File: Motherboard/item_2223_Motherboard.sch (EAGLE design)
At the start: 50 parts, among them IC1 MCP602SN, IC2 LD117AS33TR, IC4 MCP6S26, U1 ESP32-DEVKITC-32D, U2 ADS1256_BOARD, U3 SSD1306_128X64, X1 MSTBA4, X2 MSTBA4

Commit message: Correggi errore tipografico in item_2223_Motherboard.sch
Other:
- note added: "Lista Test Points: TP1 - ingresso Accel_0 TP2 - Accel_0 con bias TP3 - uscita PGA Accel_0/1 TP4 - uscita LPF Accel_0/AIN0+ TP5 - ingresso Accel_1 TP6 - Accel_1 con bias TP9 - ADC_HALF_VREF TP10 - +3V3 TP11 - +5V TP12 - GND"
- note removed: "Lista Tesp Points: TP1 - ingresso Accel_0 TP2 - Accel_0 con bias TP3 - uscita PGA Accel_0/1 TP4 - uscita LPF Accel_0/AIN0+ TP5 - ingresso Accel_1 TP6 - Accel_1 con bias TP9 - ADC_HALF_VREF TP10 - +3V3 TP11 - +5V TP12 - GND"
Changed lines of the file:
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@@
 Condizionamento coppie</text>
 <text x="346.71" y="20.32" size="2.54" layer="97">ISIS Bassa Friulana</text>
-<text x="289.56" y="33.02" size="2.1844" layer="97">Lista Tesp Points:
+<text x="289.56" y="33.02" size="2.1844" layer="97">Lista Test Points:
 TP1 - ingresso Accel_0
 TP2 - Accel_0 con bias

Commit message: Corretto GND di SSD1306 in Frontend e Motherboard
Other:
- moved on the sheet: U3
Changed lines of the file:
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@@
 <?xml version="1.0" encoding="utf-8"?>
 <!DOCTYPE eagle SYSTEM "eagle.dtd">
-<eagle version="9.6.2">
+<eagle version="7.7.0">
 <drawing>
 <settings>
 <setting alwaysvectorfont="no"/>
-<setting keepoldvectorfont="yes"/>
 <setting verticaltext="up"/>
 </settings>
-<grid distance="0.1" unitdist="inch" unit="inch" style="lines" multiple="1" display="yes" altdistance="0.01" altunitdist="inch" altunit="inch"/>
+<grid distance="0.1" unitdist="inch" unit="inch" style="lines" multiple="1" display="no" altdistance="0.01" altunitdist="inch" altunit="inch"/>
 <layers>
 <layer number="1" name="Top" color="4" fill="1" visible="no" active="no"/>

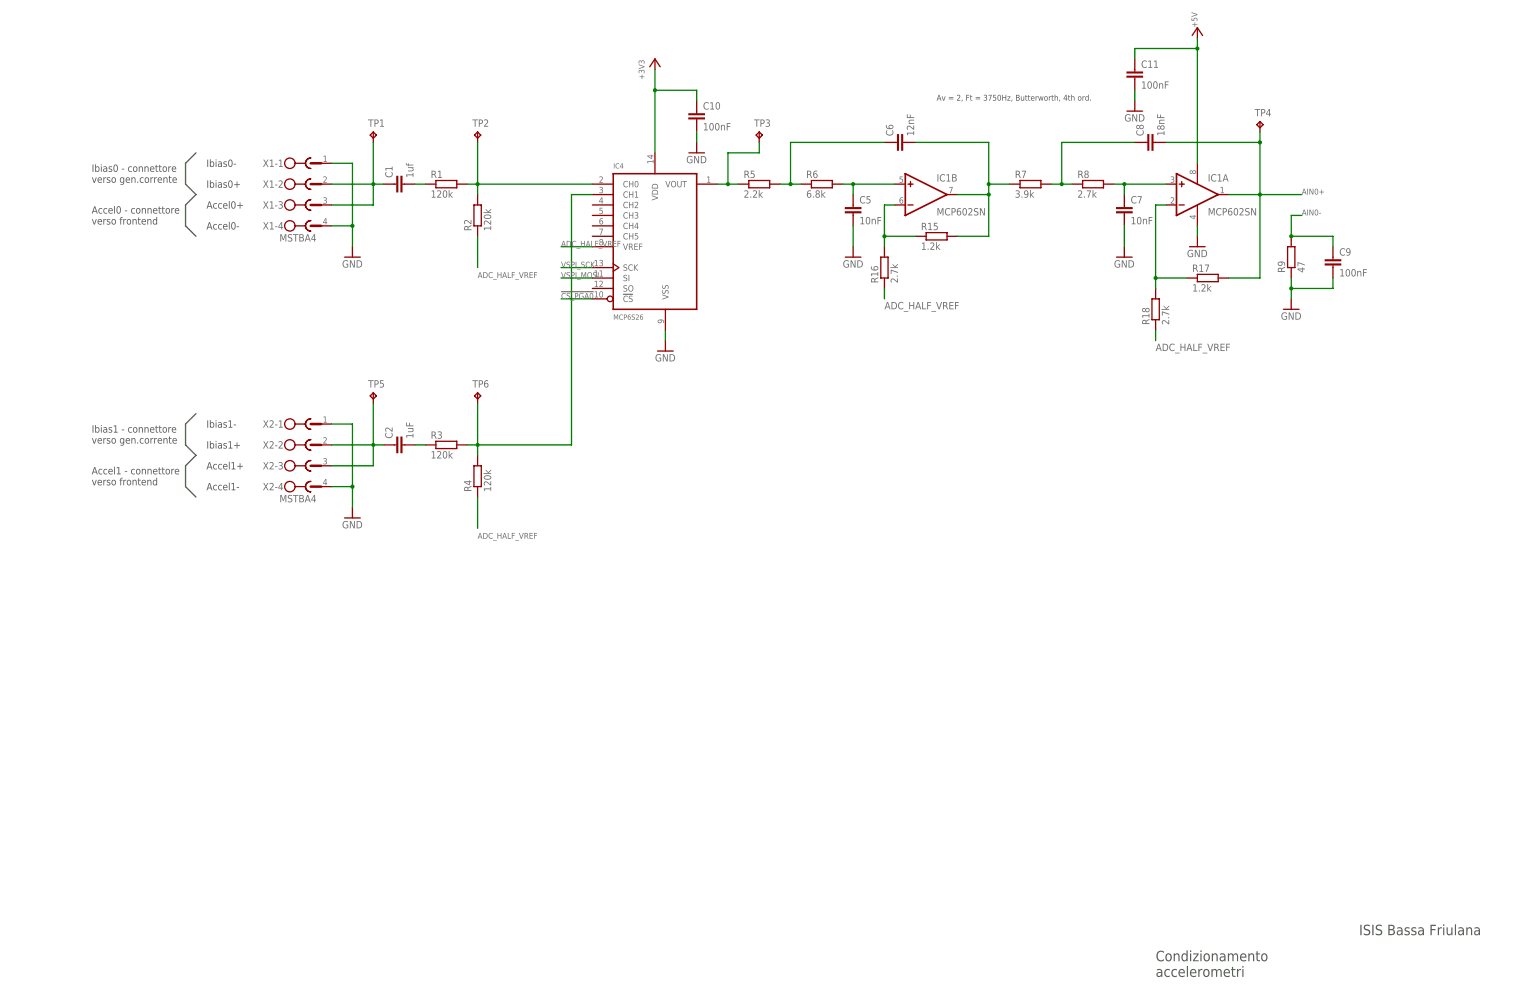
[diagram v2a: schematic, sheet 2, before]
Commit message: ingresso differenziale e AGND
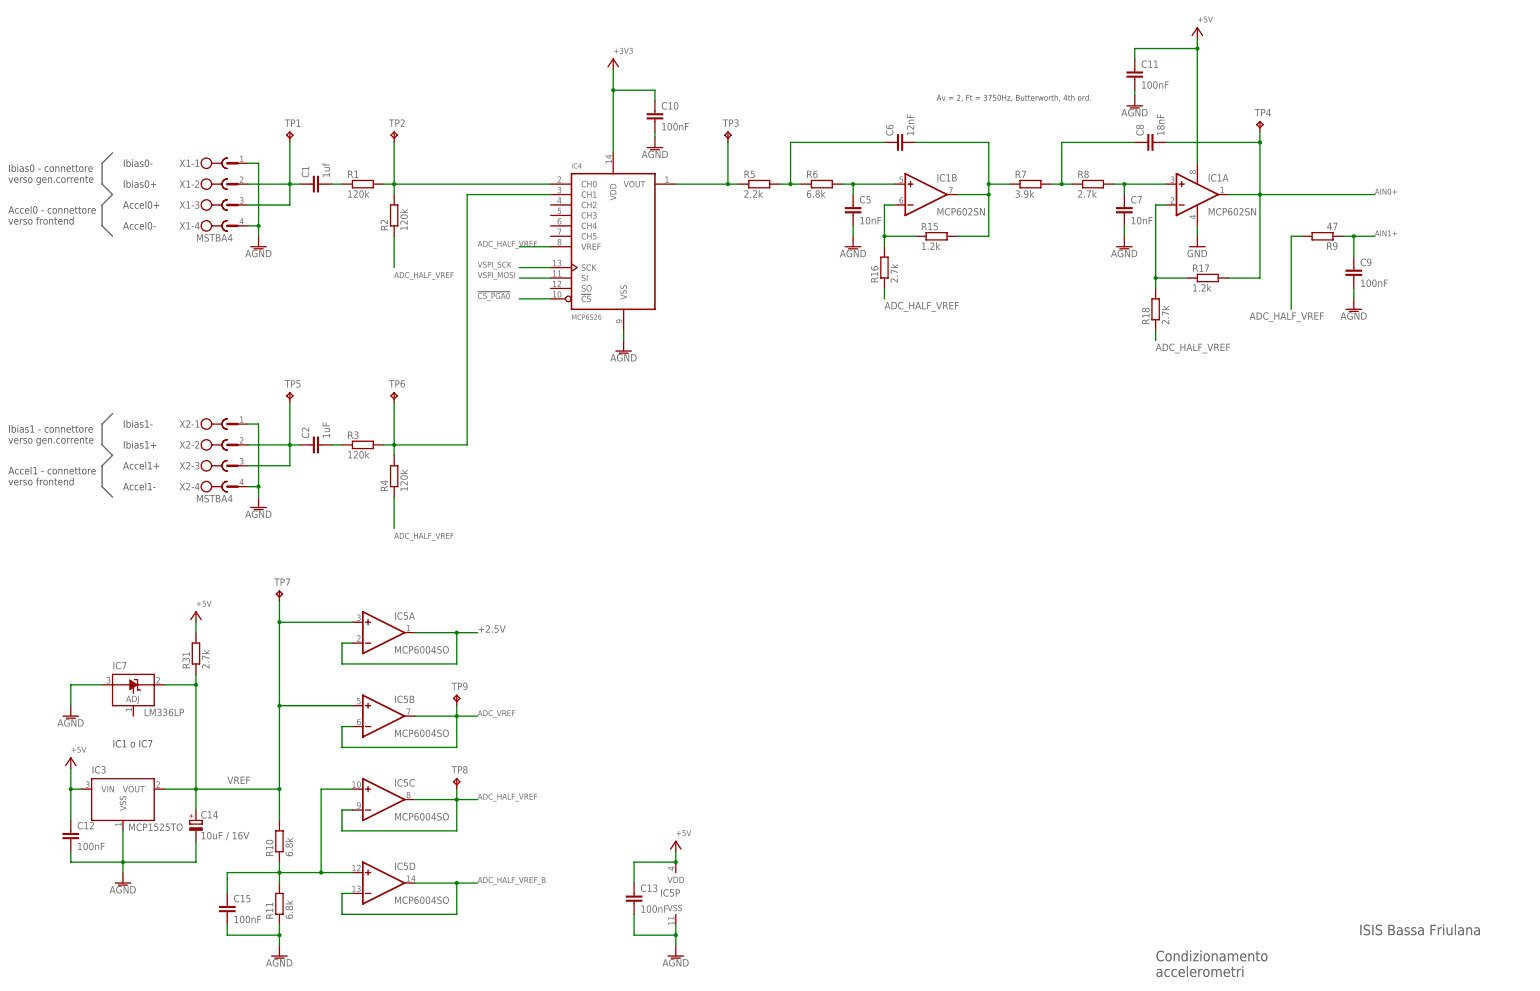
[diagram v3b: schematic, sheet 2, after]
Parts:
- added C12, C13, C15: 100nF, rcl_LargePads:C-EUC0805
- added C14: 10uF / 16V, rcl_LargePads:CPOL-EUC
- added IC3: MCP1525TO, MCP1525_MCP1541:MCP1525TO
- added IC5: MCP6004SO, MCP6002_MCP6004:MCP6004SO
- added IC7: LM336LP, linear:LM336LP
- added R10, R11: 6.8k, rcl_LargePads:R-EU_R0805
- added R31: 2.7k, rcl:R-EU_R0805
- added SJ1: (no value), jumper:SJ
- added TP7, TP8: TPTP16R, testpad:TPTP16R
- JP1: device pinhead:PINHD-1X8 -> pinhead:PINHD-1X10
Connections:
- removed net AIN0-: C9.1, R9.2, U2.AIN0-
- new net +2.5V: IC5A.-IN, IC5A.OUT, JP1.1
- new net ADC_HALF_VREF_B: IC5D.-IN, IC5D.OUT
- new net ADC_VREF: IC5B.-IN, IC5B.OUT, JP1.2, TP9.TP
- new net AGND: C10.2, C11.2, C12.2, C13.2, C14.-, C15.2, C5.2, C7.2, C9.2, IC3.VSS, IC4.VSS, IC5P.VSS, IC7.A, JP1.4, R11.1, SJ1.2, X1-1.1, X1-4.1, X2-1.1, X2-4.1
- new net AIN1+: C9.1, R9.1, U2.AIN1+
- new net N$1: C15.1, IC5C.+IN, IC5D.+IN, R10.1, R11.2
- new net VREF: C14.+, IC3.VOUT, IC5A.+IN, IC5B.+IN, IC7.C, R10.2, R31.1, TP7.TP
- net !CS_MCP3204!: now also JP1.7; no longer JP1.5
- net +3V3: now also JP1.5; no longer JP1.2
- net +5V: now also C12.1, C13.1, IC3.VIN, IC5P.VDD, R31.2
- net ADC_HALF_VREF: now also IC5C.-IN, IC5C.OUT, R9.2, TP8.TP; no longer JP1.1, TP9.TP
- net GND: now also JP1.6, SJ1.1; no longer C10.2, C11.2, C5.2, C7.2, C9.2, IC4.VSS, JP1.4, R9.1, X1-1.1, X1-4.1, X2-1.1, X2-4.1
- net VSPI_MISO: now also JP1.9; no longer JP1.7
- net VSPI_MOSI: now also JP1.10; no longer JP1.8
- net VSPI_SCK: now also JP1.8; no longer JP1.6
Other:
- note added: "IC1 o IC7"
- note added: "Lista Test Points: TP1 - ingresso Accel_0 TP2 - Accel_0 con bias TP3 - uscita PGA Accel_0/1 TP4 - uscita LPF Accel_0/AIN0+ TP5 - ingresso Accel_1 TP6 - Accel_1 con bias TP7 - VREF TP8 - ADC_HALF_VREF TP9 - ADC_VREF TP10 - +3V3 TP11 - +5V TP12 - GND"
- note added: "Punto di partenza della stella di GND/AGND da posizionare in prossimità di pin 2 di PL1"
- note removed: "Lista Test Points: TP1 - ingresso Accel_0 TP2 - Accel_0 con bias TP3 - uscita PGA Accel_0/1 TP4 - uscita LPF Accel_0/AIN0+ TP5 - ingresso Accel_1 TP6 - Accel_1 con bias TP9 - ADC_HALF_VREF TP10 - +3V3 TP11 - +5V TP12 - GND"
- moved on the sheet: C1, C10, C2, C9, IC4, R1, R2, R3, R4, R9, TP1, TP10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
